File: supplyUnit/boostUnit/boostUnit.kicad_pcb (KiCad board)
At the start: 2 copper layers, 72.7 x 33.9 mm, 26 parts, among them J1 Conn_02x03_Counter_Clockwise, J2 Conn_02x03_Counter_Clockwise

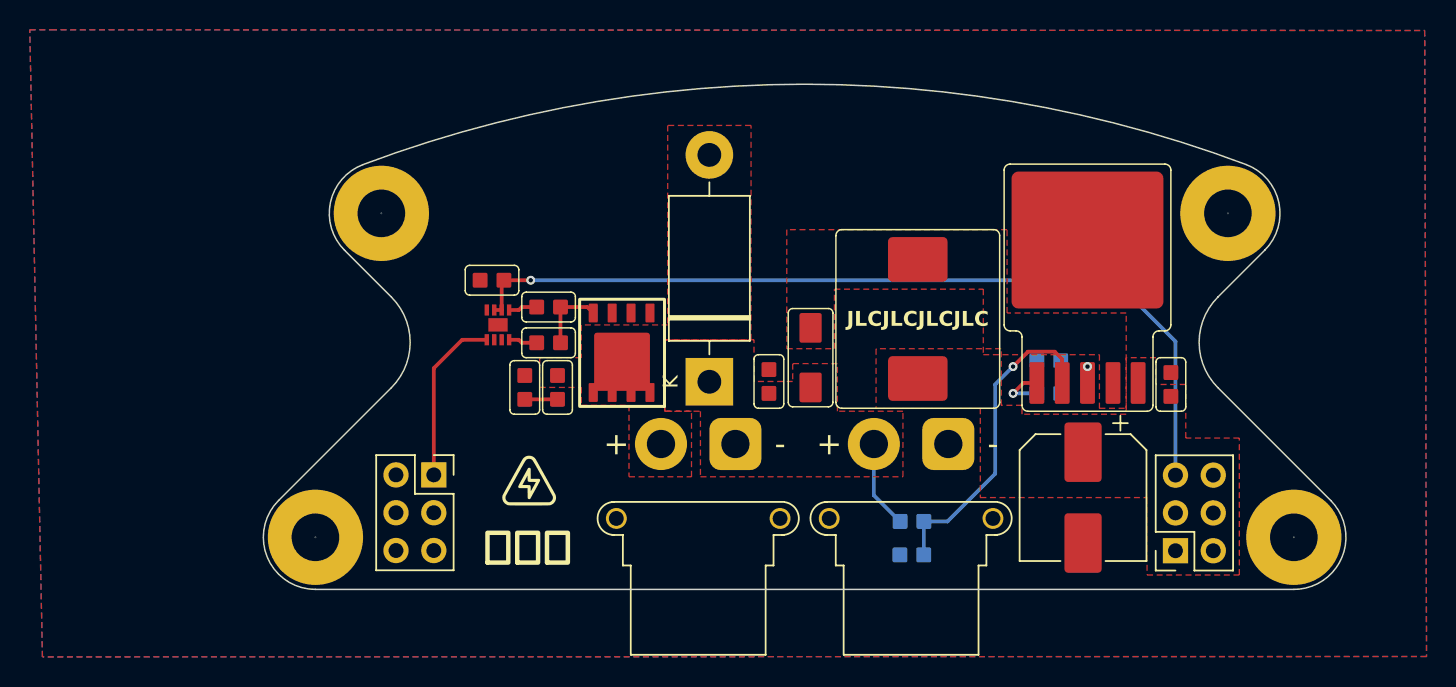
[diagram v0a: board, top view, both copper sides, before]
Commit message: new boost
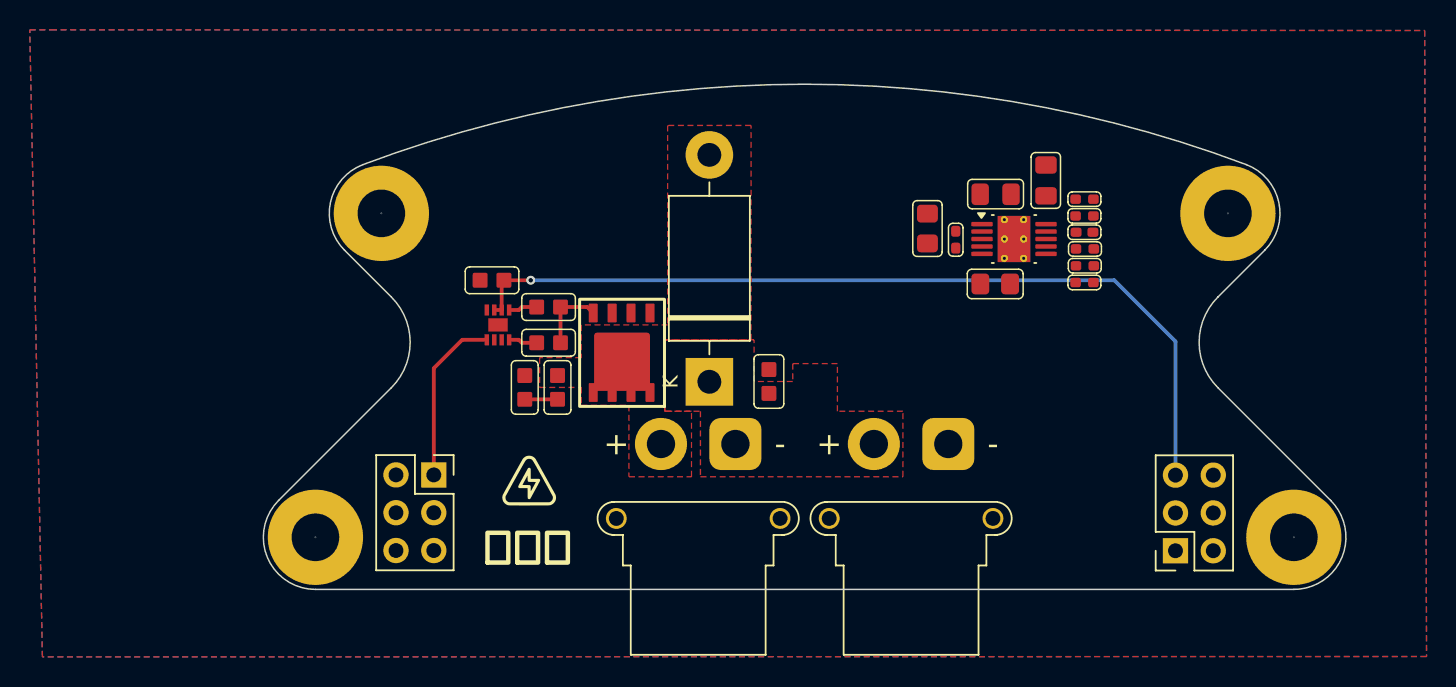
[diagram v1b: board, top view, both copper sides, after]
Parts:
- removed BC1: 0u1, Library:cap0603
- removed BC2: 100u, Capacitor_SMD:CP_Elec_8x6.5
- removed BC4: 1u, Library:cap0603
- removed BD1: SS510, Library:SMA (DO-214AC)
- removed BIC1: LM2587S-ADJ, Library:TO170P1435X465-6N
- removed BL1: 68uH, Library:1040 One Piece Inductor
- removed BR1: 57K, Library:res0603
- removed BR2: 2k94, Library:res0603
- removed BR3: 1K5, Library:res0603
- added C1: 2.2uF, Boost:cap0805, F.Cu at (150.0, 91.8)
- added C2: 0.1uF, Boost:cap0402, F.Cu at (147.3, 94.9)
- added C3: 0.01uF, Boost:cap0402, F.Cu at (156.0, 94.4)
- added C4: 2.2uF, Boost:cap0805, F.Cu at (153.4, 90.9)
- added C5: 4.7uF, Boost:res0805, F.Cu at (150.0, 97.8)
- added L1: 10uH, Boost:res0805, F.Cu at (145.4, 94.1)
- added R1: 1M, Boost:res0402, F.Cu at (156.0, 95.5)
- added R2: 162K, Boost:res0402, F.Cu at (156.0, 96.6)
- added R3: 40.2K, Boost:res0402, F.Cu at (156.0, 97.7)
- added R4: 1M, Boost:res0402, F.Cu at (156.0, 93.2)
- added R5: 953K, Boost:res0402, F.Cu at (156.0, 92.1)
- added U1: ~, Boost:LT8338, F.Cu at (151.2, 94.8)
- BSC1, BSR1, BSR2, BSR3: footprint Library:res0603 -> Boost:res0603
- BSC2: footprint Library:cap0603 -> Boost:cap0603
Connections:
- BSD1 pad 1: +48V -> +24V
- BSJ1 pad 1: +48V -> +24V
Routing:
- net Net-(BIC1-FDBK): track 21.6 -> 0.00 mm, vias 1 -> 0
- net +48V: track 5.93 -> 0.00 mm
- net Net-(BIC1-COMP): track 3.49 -> 0.00 mm, vias 1 -> 0
- net Net-(BC4-Pad1): track 2.20 -> 0.00 mm
- net GND: vias 1 -> 0
- added copper zone on F.Cu, net +24V
- removed copper zone on F.Cu, net +12V
- removed copper zone on F.Cu, net +48V
- removed copper zone on F.Cu, net Net-(BD1-A)
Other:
- board text removed: "JLCJLCJLCJLC"

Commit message: trial routing
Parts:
- moved C1 6.01 mm to (151.5, 97.6)
- moved C4 6.01 mm to (154.9, 96.7)
- moved C5 6.01 mm to (151.5, 103.7)
- moved R1 6.01 mm to (157.5, 101.3)
- moved R2 6.01 mm to (157.5, 102.4)
- moved R3 6.01 mm to (157.5, 103.5)
- moved C2 6.01 mm to (148.8, 100.7)
- moved C3 6.01 mm to (157.5, 100.2)
- moved L1 6.01 mm to (146.9, 99.9)
- moved R4 6.01 mm to (157.5, 99.1)
- moved R5 6.01 mm to (157.5, 97.9)
- moved U1 6.01 mm to (152.7, 100.6)
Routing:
- net +12V: track 58.1 -> 89.7 mm, vias 1 -> 3
- net Net-(U1-CTRL): track 0.00 -> 4.80 mm
- net Net-(U1-INTVCC): track 0.00 -> 3.98 mm
- net Net-(U1-RT): track 0.00 -> 3.69 mm
- net Net-(U1-EN/UVLO): track 0.00 -> 3.42 mm
- added copper zone on B.Cu, net +12V
- added copper zone on F.Cu, net +12V
- added copper zone on F.Cu, net Net-(U1-BST)
- added copper zone on F.Cu, net SW

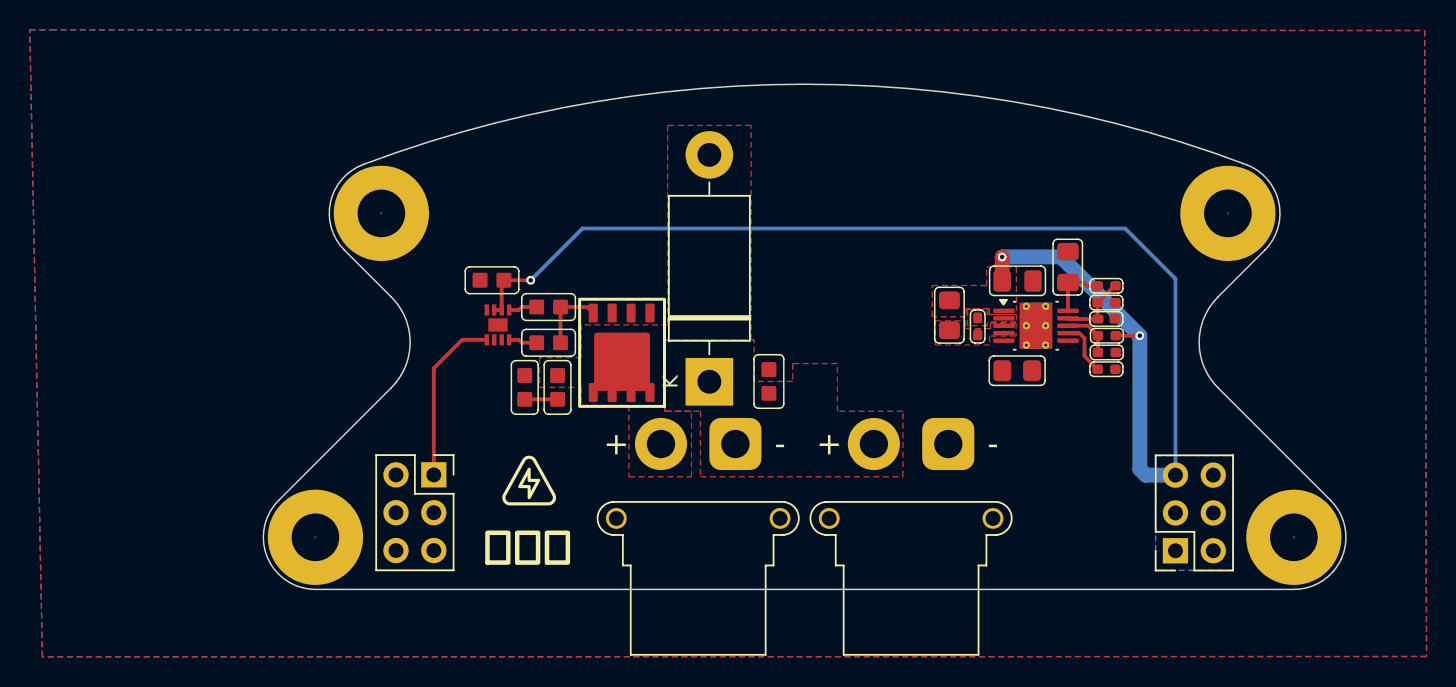
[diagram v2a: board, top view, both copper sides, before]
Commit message: boost routing
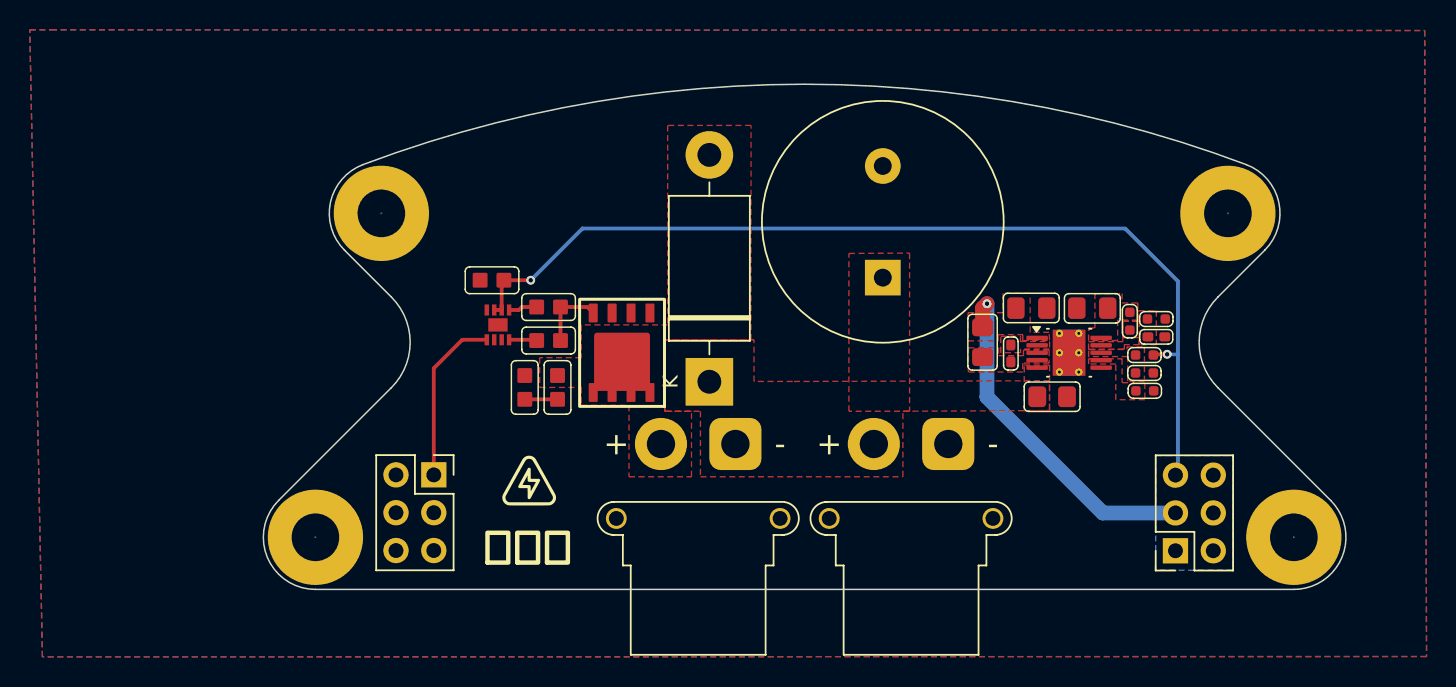
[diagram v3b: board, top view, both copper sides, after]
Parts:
- removed BC3: 0u1, Library:cap0603
- added C6: 1500uF, Boost:CP_Radial_D16.0mm_P7.50mm, F.Cu at (142.4, 93.7)
- moved C3 3.56 mm to (160.8, 101.4)
- moved R4 3.53 mm to (160.8, 100.2)
- moved C4 3.21 mm to (156.5, 99.5), turned to 180 degrees
- moved R3 2.96 mm to (160.0, 105.0)
- moved C5 2.93 mm to (153.8, 105.4)
- moved R5 2.88 mm to (159.1, 100.3), turned to -90 degrees
- moved R2 2.88 mm to (160.0, 103.8)
- moved C2 2.87 mm to (151.0, 102.5)
- moved L1 2.87 mm to (149.1, 101.7)
- moved U1 2.87 mm to (154.9, 102.5)
- moved R1 2.84 mm to (160.0, 102.6)
- moved C1 2.05 mm to (152.4, 99.5)
- moved BSR3 0.15 mm to (120.0, 101.6)
- renumbered BJ1 to BSJ2
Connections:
- BSJ2 pad 2: +48V -> +24V
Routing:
- net Net-(U1-CTRL): track 4.80 -> 0.00 mm
- net Net-(U1-INTVCC): track 3.98 -> 0.01 mm
- net Net-(U1-RT): track 3.69 -> 0.00 mm
- net Net-(U1-EN/UVLO): track 3.42 -> 0.00 mm
- added copper zone on F.Cu, net Net-(U1-CTRL)
- added copper zone on F.Cu, net Net-(U1-EN/UVLO)
- added copper zone on F.Cu, net Net-(U1-INTVCC)
- added copper zone on F.Cu, net Net-(U1-RT)

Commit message: boost
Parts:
- moved R4 0.70 mm to (161.4, 99.7)
- moved C3 0.59 mm to (161.4, 101.2)
- moved R3 0.50 mm to (160.0, 105.5)
- moved R5 0.29 mm to (159.3, 100.2)
- moved R2 0.25 mm to (160.0, 104.0)
- moved C1 0.18 mm to (152.3, 99.5)
- moved L1 0.10 mm to (149.0, 101.7)
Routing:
- net +12V: track 89.3 -> 71.8 mm, vias 3 -> 2

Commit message: Fab
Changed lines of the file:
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@@
 				(font
 					(size 1.27 1.27)
+					(thickness 0.15)
 				)
 			)
@@
 				(font
 					(size 1.27 1.27)
+					(thickness 0.15)
 				)
 			)
@@
 				(font
 					(size 1.27 1.27)
+					(thickness 0.15)
 				)
 			)
@@
 		(fp_arc
 			(start 1.5 -0.973553)
-			(mid 1.853554 -0.827107)
+			(mid 1.853551 -0.827106)
 			(end 2 -0.473553)
 			(stroke
@@
 				(font
 					(size 1.27 1.27)
+					(thickness 0.15)
 				)
 			)
@@
 				(font
 					(size 1.27 1.27)
+					(thickness 0.15)
 				)
 			)
@@
 				(font
 					(size 1.27 1.27)
+					(thickness 0.15)
 				)
 			)
@@
 		(fp_arc
 			(start 1.5 -0.973553)
-			(mid 1.853554 -0.827107)
+			(mid 1.853551 -0.827106)
 			(end 2 -0.473553)
 			(stroke
@@
 				(font
 					(size 1.27 1.27)
+					(thickness 0.15)
 				)
 			)
@@
 				(font
 					(size 1.27 1.27)
+					(thickness 0.15)
 				)
 			)
@@
 				(font
 					(size 1.27 1.27)
+					(thickness 0.15)
 				)
 			)
@@
 				(font
 					(size 1.27 1.27)
+					(thickness 0.15)
 				)
 			)
@@
 				(font
 					(size 1.27 1.27)
+					(thickness 0.15)
 				)
 			)
@@
 				(font
 					(size 1.27 1.27)
+					(thickness 0.15)
 				)
 			)
@@
 				(font
 					(size 1.27 1.27)
+					(thickness 0.15)
 				)
 			)
@@
 				(font
 					(size 1.27 1.27)
+					(thickness 0.15)
 				)
 			)
@@
 				(font
 					(size 1.27 1.27)
+					(thickness 0.15)
 				)
 			)
@@
 				(font
 					(size 1.27 1.27)
+					(thickness 0.15)
 				)
 			)
@@
 				(font
 					(size 1.27 1.27)
+					(thickness 0.15)
 				)
 			)
@@
 				(font
 					(size 1.27 1.27)
+					(thickness 0.15)
 				)
 			)
@@
 				(font
 					(size 1.27 1.27)
+					(thickness 0.15)
 				)
 			)
@@
 				(font
 					(size 1.27 1.27)
+					(thickness 0.15)
 				)
 			)
@@
 				(font
 					(size 1.27 1.27)
+					(thickness 0.15)
 				)
 			)
@@
 		(polygon
 			(pts
-				(xy 144.230978 95.758123) (xy 144.230978 106.383123) (xy 140.155978 106.383123) (xy 140.155978 95.783123)
+				(xy 144.230978 95.758123) (xy 144.230978 106.383123) (xy 140.755978 106.383123) (xy 140.755978 95.783123)
 			)
 		)

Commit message: Revert
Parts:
- removed C1, C4: 2.2uF, Boost:cap0805
- removed C2: 0.1uF, Boost:cap0402
- removed C3: 0.01uF, Boost:cap0402
- removed C5: 4.7uF, Boost:res0805
- removed C6: 1500uF, Boost:CP_Radial_D16.0mm_P7.50mm
- removed L1: 10uH, Boost:res0805
- removed R1, R4: 1M, Boost:res0402
- removed R2: 162K, Boost:res0402
- removed R3: 40.2K, Boost:res0402
- removed R5: 953K, Boost:res0402
- removed U1: ~, Boost:LT8338
- added BC1: 0u1, Library:cap0603, F.Cu at (161.8, 104.6)
- added BC2: 100u, Capacitor_SMD:CP_Elec_8x6.5, F.Cu at (155.9, 112.2)
- added BC3: 0u1, Library:cap0603, F.Cu at (134.8, 104.4)
- added BC4: 1u, Library:cap0603, B.Cu at (153.6, 103.0)
- added BD1: SS510, Library:SMA (DO-214AC), F.Cu at (137.6, 102.8)
- added BIC1: LM2587S-ADJ, Library:TO170P1435X465-6N, F.Cu at (156.2, 101.4)
- added BL1: 68uH, Library:1040 One Piece Inductor, F.Cu at (144.8, 100.2)
- added BR1: 57K, Library:res0603, B.Cu at (144.4, 113.8)
- added BR2: 2k94, Library:res0603, B.Cu at (153.6, 105.2)
- added BR3: 1K5, Library:res0603, B.Cu at (144.4, 116.0)
- BSC1, BSR1, BSR2, BSR3: footprint Boost:res0603 -> Library:res0603
- BSC2: footprint Boost:cap0603 -> Library:cap0603
- moved BSR3 0.15 mm to (120.0, 101.8)
- renumbered BSJ2 to BJ1
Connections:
- net +24V renamed +48V
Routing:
- net Net-(BIC1-FDBK): track 0.00 -> 21.6 mm, vias 0 -> 1
- net +12V: track 71.8 -> 58.1 mm, vias 2 -> 1
- net +48V: track 0.00 -> 5.93 mm
- net Net-(BIC1-COMP): track 0.00 -> 3.49 mm, vias 0 -> 1
- net Net-(BC4-Pad1): track 0.00 -> 2.20 mm
- net GND: vias 0 -> 1
- added copper zone on F.Cu, net Net-(BD1-A)
- removed copper zone on B.Cu, net +12V
- removed copper zone on F.Cu, net Net-(U1-BST)
- removed copper zone on F.Cu, net Net-(U1-CTRL)
- removed copper zone on F.Cu, net Net-(U1-EN/UVLO)
- removed copper zone on F.Cu, net Net-(U1-INTVCC)
- removed copper zone on F.Cu, net Net-(U1-RT)
- removed copper zone on F.Cu, net SW

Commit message: 死
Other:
- board text added: "JLCJLCJLCJLC"
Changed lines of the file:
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@@
+		)
+	)
+	(gr_text "JLCJLCJLCJLC"
+		(at 144.780978 100.183123 0)
+		(layer "F.SilkS")
+		(effects
+			(font
+				(size 1 1)
+				(thickness 0.25)
+				(bold yes)
+			)
 		)
 	)
